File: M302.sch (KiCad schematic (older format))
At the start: 28 parts, among them J1 I2C-SHT3x, J2 I2C-ThmCp, J3 I2C-3, J4 I2C-4, J5 I2C-D400, J6 W5500, J7 IM920, J8 PWR+5V, J9 ANALOG-IN, P1 Power, P2 Analog, P3 Digital, P4 Digital, P5 CONN_01X01, P6 CONN_01X01, P7 CONN_01X01, P8 CONN_01X01, SW1 CPU, SW2 D400, SW3 IM920, U1 SFE-BOB-12009

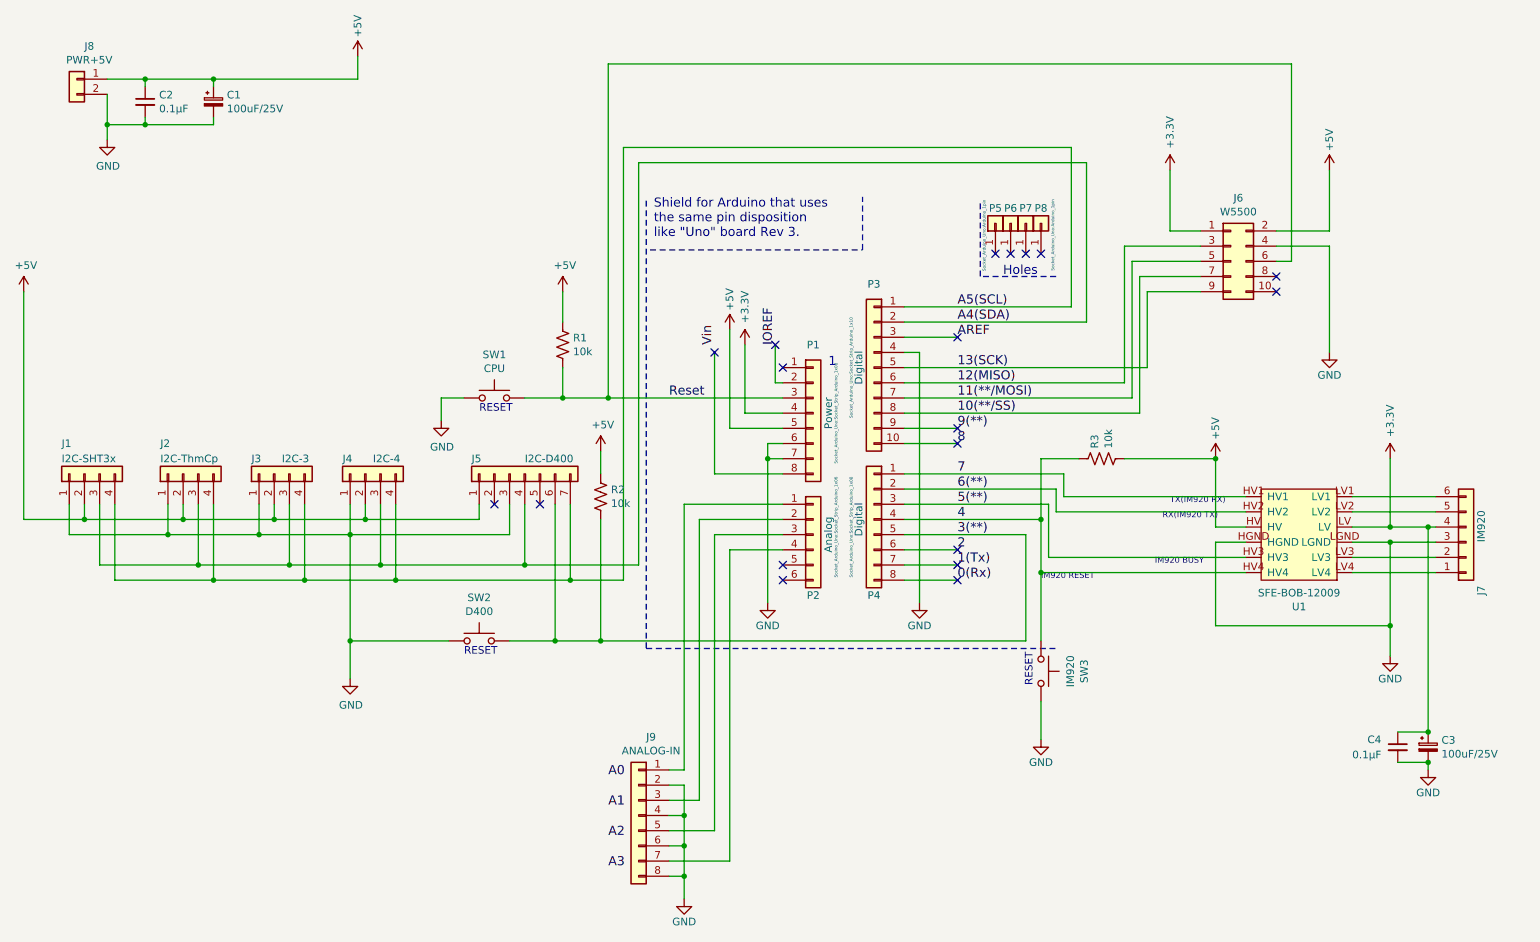
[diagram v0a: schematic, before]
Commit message: M302J PCB途中. Ethernet Moduleのpin配置不明
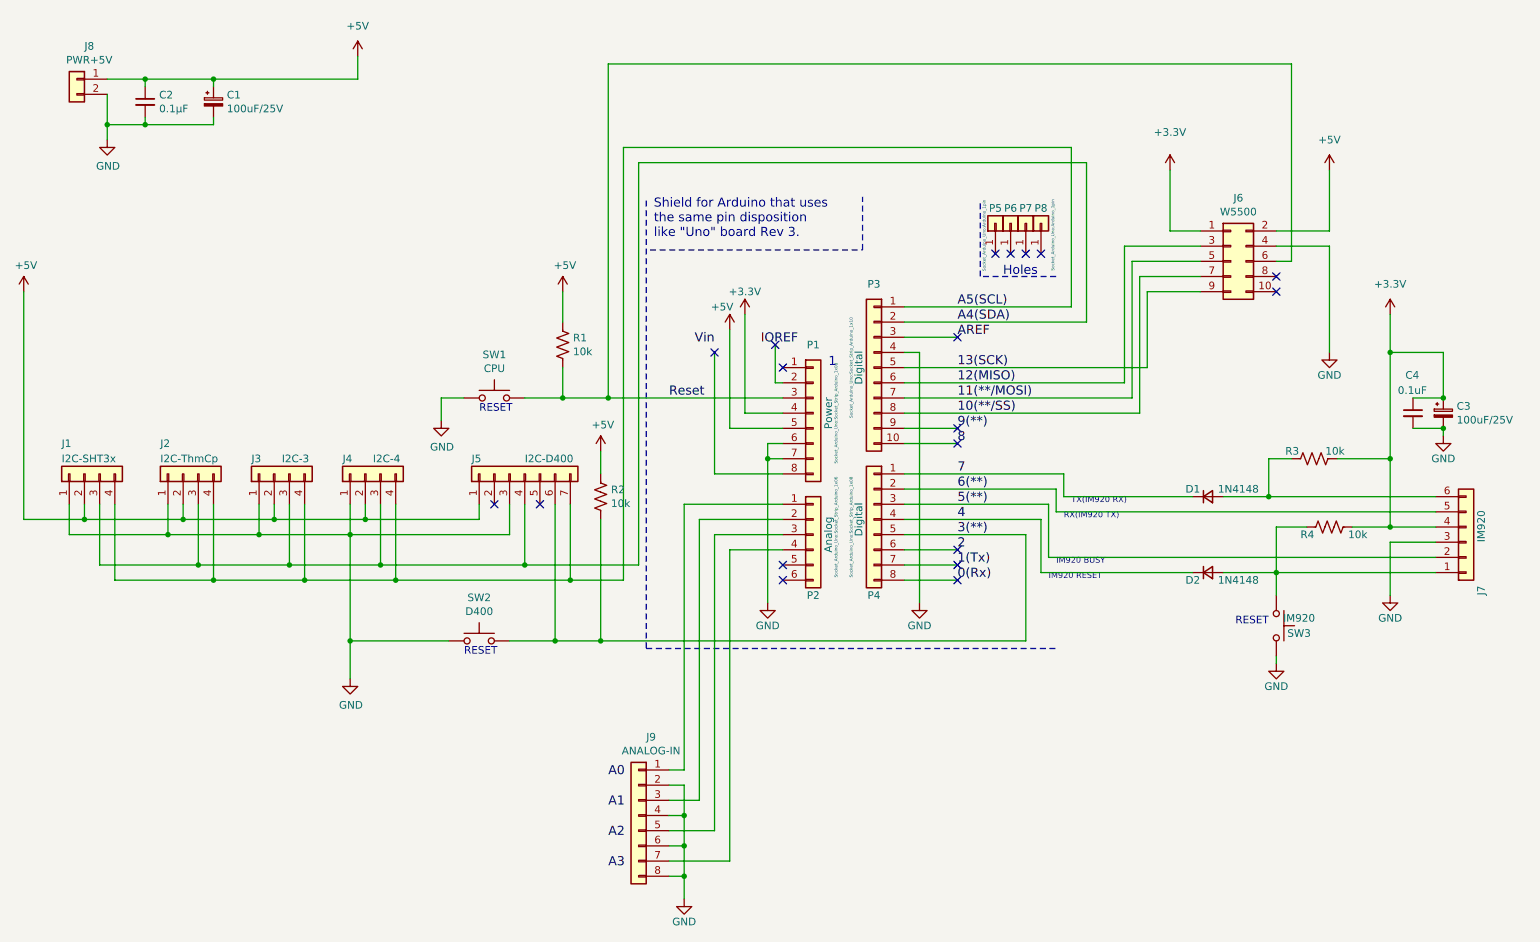
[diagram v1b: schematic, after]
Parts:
- removed U1: SFE-BOB-12009, HOLLY:SFE-BOB-12009, symbol Buffer:SFE-BOB-12009
- added D1, D2: 1N4148, Diode_THT:D_DO-35_SOD27_P2.54mm_Vertical_AnodeUp, symbol Device:D_Small
- added R4: 10k, Resistor_THT:R_Axial_DIN0207_L6.3mm_D2.5mm_P2.54mm_Vertical, symbol Device:R_US
- C4: value 0.1μF -> 0.1uF
- R1, R2, R3: footprint Resistor_THT:R_Axial_DIN0207_L6.3mm_D2.5mm_P7.62mm_Horizontal -> Resistor_THT:R_Axial_DIN0207_L6.3mm_D2.5mm_P2.54mm_Vertical
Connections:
- net +3V3: now also R3.2, R4.2
- net +5V: no longer R3.2
- net 4: now also D2.1 (K); no longer R3.1, SW3.1
- net 5(**): now also J7.2 (Pin_2)
- net 6(**): now also J7.5 (Pin_5)
- net 7: now also D1.1 (K)
- net IOREF: no longer P1.2 (Pin_2)
- net at J7.6 (Pin_6): now also R3.1, D1.2 (A)
- net at J7.1 (Pin_1): now also SW3.1, D2.2 (A), R4.1
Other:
- moved on the sheet: C3, C4, R3, SW3
